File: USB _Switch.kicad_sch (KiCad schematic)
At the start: 21 parts

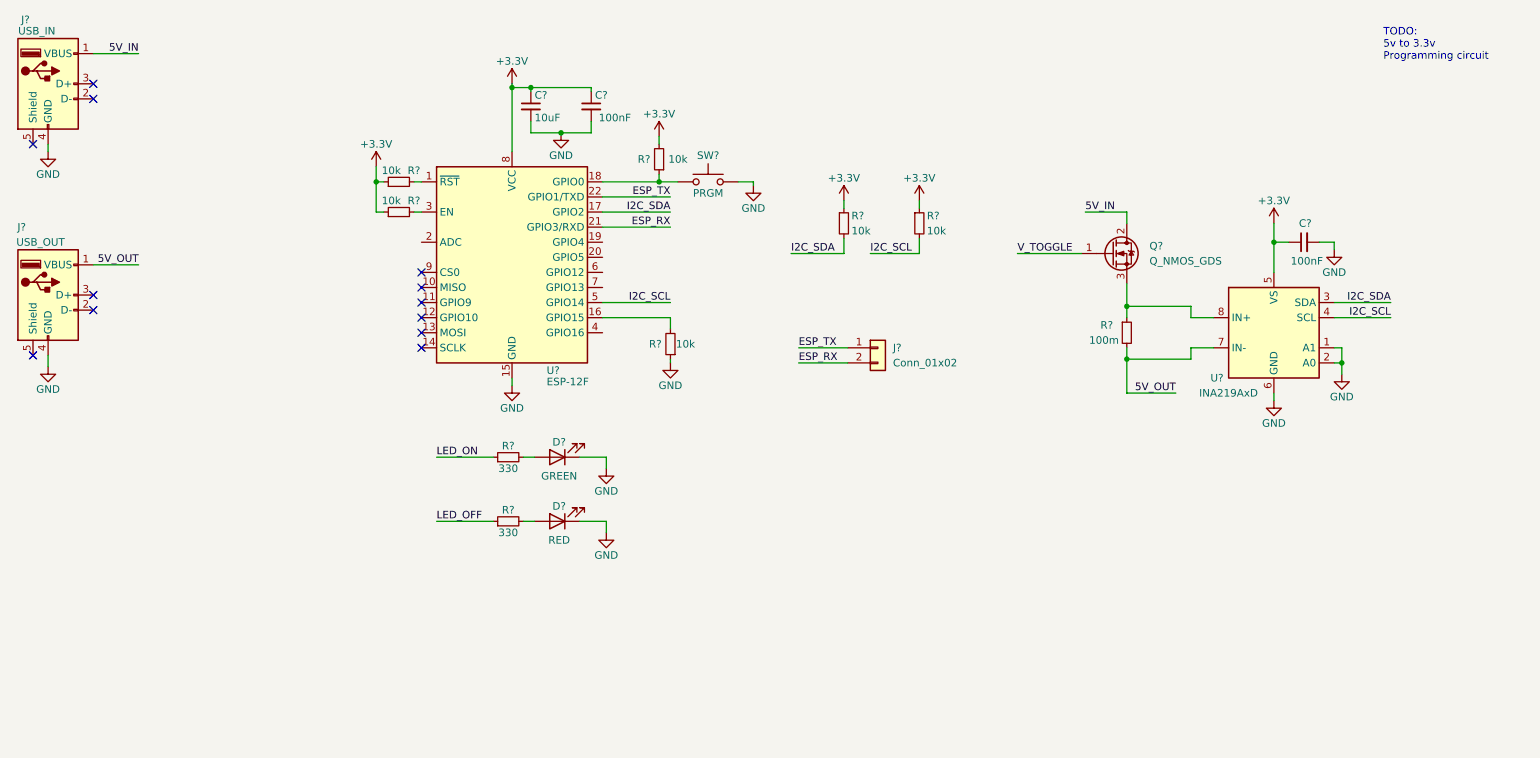
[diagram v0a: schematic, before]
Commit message: Split schematic into two sheets
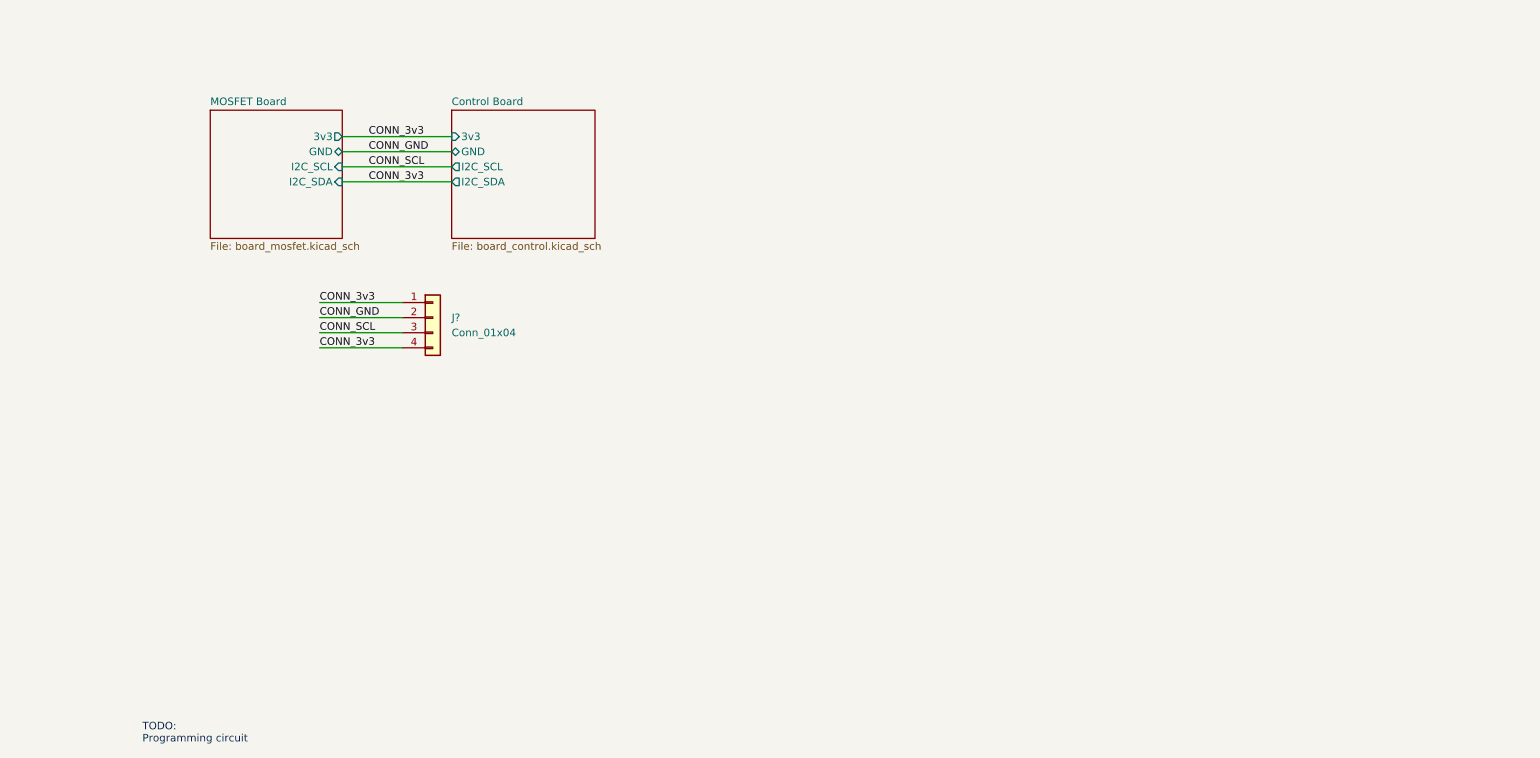
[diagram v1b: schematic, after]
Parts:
- removed C? (x2): 100nF, symbol Device:C_Small
- removed C?: 10uF, symbol Device:C_Small
- removed D?: GREEN, symbol Device:LED
- removed D?: RED, symbol Device:LED
- removed J?: USB_OUT, symbol Connector:USB_A
- removed J?: USB_IN, symbol Connector:USB_A
- removed J?: Conn_01x02, symbol Connector_Generic:Conn_01x02
- removed Q?: Q_NMOS_GDS, symbol Device:Q_NMOS_GDS
- removed R? (x2): 330, symbol Device:R_Small
- removed R? (x6): 10k, symbol Device:R_Small
- removed R?: 100m, symbol Device:R_Small
- removed SW?: PRGM, symbol Switch:SW_Push
- removed U?: ESP-12F, RF_Module:ESP-12E, symbol RF_Module:ESP-12F
- removed U?: INA219AxD, Package_SO:SOIC-8_3.9x4.9mm_P1.27mm, symbol Analog_ADC:INA219AxD
- added J?: Conn_01x04, symbol Connector_Generic:Conn_01x04
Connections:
- new net CONN_3v3: J?.1 (Pin_1), J?.4 (Pin_4)
- new net CONN_GND: J?.2 (Pin_2)
- new net CONN_SCL: J?.3 (Pin_3)
- no-connect marks 12 -> 0
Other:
- added sheet Control Board (board_control.kicad_sch)
- added sheet MOSFET Board (board_mosfet.kicad_sch)
- note added: "TODO: Programming circuit"
- note removed: "TODO: 5v to 3.3v Programming circuit"
